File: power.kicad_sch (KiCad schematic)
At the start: 29 parts, among them IC302 L7805, IC303 L7805, Q503 BR 29, SW101 SW_SPDT

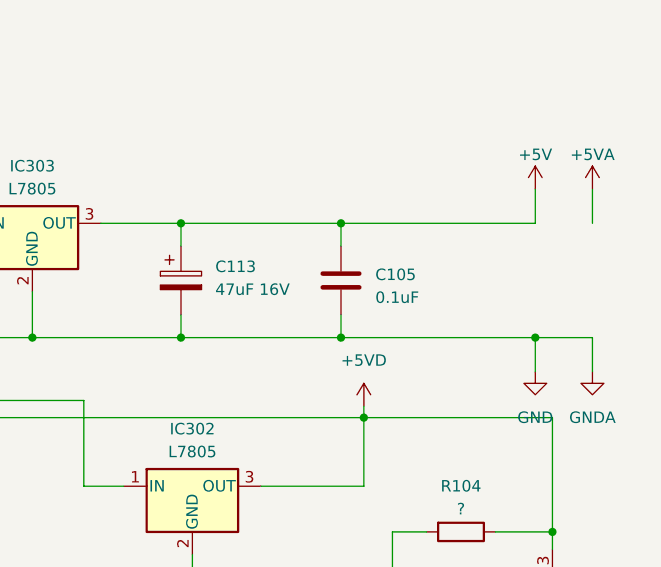
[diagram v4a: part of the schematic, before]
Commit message: IC routing mostly complete, start adding passives.
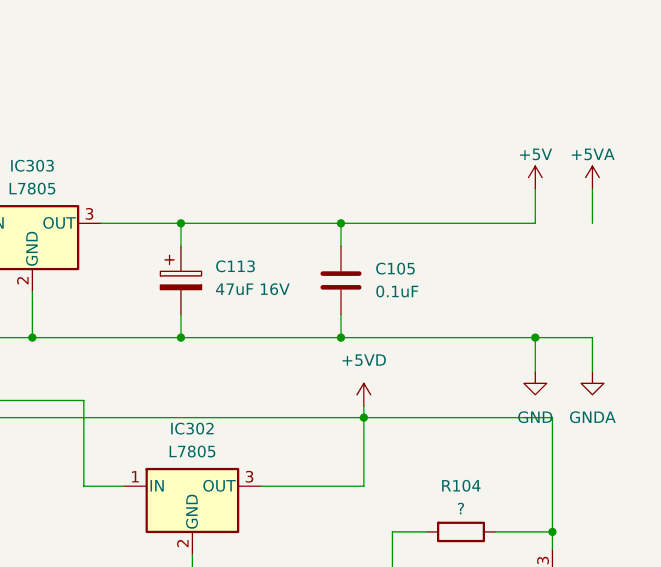
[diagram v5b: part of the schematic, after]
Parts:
- C105: footprint Capacitor_SMD:C_0805_2012Metric -> A-PCENGINE:SMD_0805_Narrow
- R104: footprint Resistor_SMD:R_0805_2012Metric -> A-PCENGINE:SMD_0805_Narrow
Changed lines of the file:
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@@
   (symbol (lib_id "Device:C") (at 287.02 57.15 0) (unit 1)
     (in_bom yes) (on_board yes) (dnp no) (fields_autoplaced)
-    (property "Reference" "C105" (at 290.83 56.515 0)
-      (effects (font (size 1.27 1.27)) (justify left))
-    )
-    (property "Value" "0.1uF" (at 290.83 59.055 0)
-      (effects (font (size 1.27 1.27)) (justify left))
-    )
-    (property "Footprint" "Capacitor_SMD:C_0805_2012Metric" (at 287.9852 60.96 0)
+    (property "Reference" "C105" (at 290.83 55.88 0)
+      (effects (font (size 1.27 1.27)) (justify left))
+    )
+    (property "Value" "0.1uF" (at 290.83 58.42 0)
+      (effects (font (size 1.27 1.27)) (justify left))
+    )
+    (property "Footprint" "A-PCENGINE:SMD_0805_Narrow" (at 287.9852 60.96 0)
       (effects (font (size 1.27 1.27)) hide)
     )
@@
         )
         (path "/c1c718c6-a427-431e-a18b-e46f94ae8e09/ba362b1f-3cb7-4861-9385-2b05dca17551"
-          (reference "C118") (unit 1)
+          (reference "Cx118") (unit 1)
         )
       )
@@
       (effects (font (size 1.27 1.27)) (justify left))
     )
-    (property "Footprint" "Capacitor_SMD:C_0805_2012Metric" (at 276.5552 139.7 0)
+    (property "Footprint" "A-PCENGINE:SMD_0805_Narrow" (at 276.5552 139.7 0)
       (effects (font (size 1.27 1.27)) hide)
     )
@@
       (effects (font (size 1.27 1.27)) (justify left))
     )
-    (property "Footprint" "Capacitor_SMD:C_0805_2012Metric" (at 235.9152 60.96 0)
+    (property "Footprint" "A-PCENGINE:SMD_0805_Narrow" (at 235.9152 60.96 0)
       (effects (font (size 1.27 1.27)) hide)
     )
@@
       (effects (font (size 1.27 1.27)) (justify left))
     )
-    (property "Footprint" "Capacitor_SMD:C_0805_2012Metric" (at 276.5552 125.73 0)
+    (property "Footprint" "A-PCENGINE:SMD_0805_Narrow" (at 276.5552 125.73 0)
       (effects (font (size 1.27 1.27)) hide)
     )
@@
       (effects (font (size 1.27 1.27)))
     )
-    (property "Footprint" "Resistor_SMD:R_0805_2012Metric" (at 300.355 83.312 90)
+    (property "Footprint" "A-PCENGINE:SMD_0805_Narrow" (at 300.355 83.312 90)
       (effects (font (size 1.27 1.27)) hide)
     )
@@
         )
         (path "/c1c718c6-a427-431e-a18b-e46f94ae8e09/ba362b1f-3cb7-4861-9385-2b05dca17551"
-          (reference "L105") (unit 1)
+          (reference "LX105") (unit 1)
         )
       )
@@
       (effects (font (size 1.27 1.27)) (justify left))
     )
-    (property "Footprint" "Capacitor_SMD:C_0805_2012Metric" (at 126.6952 60.96 0)
+    (property "Footprint" "A-PCENGINE:SMD_0805_Narrow" (at 126.6952 60.96 0)
       (effects (font (size 1.27 1.27)) hide)
     )
@@
       (effects (font (size 1.27 1.27)) (justify left))
     )
-    (property "Footprint" "Capacitor_SMD:C_0805_2012Metric" (at 221.9452 133.35 0)
+    (property "Footprint" "A-PCENGINE:SMD_0805_Narrow" (at 221.9452 133.35 0)
       (effects (font (size 1.27 1.27)) hide)
     )
@@
       (effects (font (size 1.27 1.27)))
     )
-    (property "Footprint" "Resistor_SMD:R_0805_2012Metric" (at 266.7 127.762 90)
-      (effects (font (size 1.27 1.27)) hide)
-    )
+    (property "Footprint" "A-PCENGINE:SMD_0805_Narrow" (at 266.7 127.762 90)
+      (effects (font (size 1.27 1.27)) hide)
+    )

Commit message: Bunch of passives and what-not.
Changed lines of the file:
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@@
   (junction (at 200.66 63.5) (diameter 0) (color 0 0 0 0)
+  )
+  (junction (at 308.61 50.8) (diameter 0) (color 0 0 0 0)
   )
   (junction (at 147.32 158.75) (diameter 0) (color 0 0 0 0)
@@
   )
   (wire (pts (xy 125.73 60.96) (xy 125.73 63.5))
+    (stroke (width 0) (type default))
+  )
+  (wire (pts (xy 308.61 50.8) (xy 314.96 50.8))
     (stroke (width 0) (type default))
   )
@@
   (symbol (lib_id "Device:D") (at 162.56 50.8 180) (unit 1)
     (in_bom yes) (on_board yes) (dnp no) (fields_autoplaced)
-    (property "Reference" "D101" (at 162.56 45.72 0)
-      (effects (font (size 1.27 1.27)))
-    )
-    (property "Value" "IS954" (at 162.56 48.26 0)
+    (property "Reference" "D101" (at 162.56 44.45 0)
+      (effects (font (size 1.27 1.27)))
+    )
+    (property "Value" "IS954" (at 162.56 46.99 0)
       (effects (font (size 1.27 1.27)))
     )
@@
         )
         (path "/c1c718c6-a427-431e-a18b-e46f94ae8e09/ba362b1f-3cb7-4861-9385-2b05dca17551"
-          (reference "D102") (unit 1)
-        )
-      )
+          (reference "D301") (unit 1)
+        )
+      )

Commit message: More passives, custom footprints, etc.
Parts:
- removed C113: 47uF 16V, A-PCENGINE:Elec_P5.00mm, symbol Device:C_Polarized
- added C105: ?, A-PCENGINE:SMD_0805_Narrow, symbol Device:C
- added C113: ?, A-PCENGINE:Elec_P5.00mm_D10.5mm, symbol Device:C_Polarized
- added C113: ?, A-PCENGINE:Elec_P5.00mm_D8.5mm, symbol Device:C_Polarized
- added C113: ?, A-PCENGINE:CP_8x2mm, symbol Device:C_Polarized
- added Q304: ~, A-PCENGINE:Transistor_SMD, symbol Device:Q_NPN_CBE
- C105, R104: footprint A-PCENGINE:SMD_0805_Narrow -> A-PCENGINE:SMD_0805_Narrow_Long
- C113: footprint A-PCENGINE:Elec_P5.00mm -> A-PCENGINE:Elec_P5.00mm_D8.5mm
- C113: footprint A-PCENGINE:Elec_P5.00mm -> A-PCENGINE:Elec_P5.00mm_D12.5mm
- C113: footprint A-PCENGINE:Elec_P5.00mm -> A-PCENGINE:Elec_P5.00mm_D7mm
- C113: footprint A-PCENGINE:Elec_P5.00mm -> A-PCENGINE:Elec_P5.00mm_D10.5mm
- IC302, IC303: footprint Connector_PinHeader_2.54mm:PinHeader_1x03_P2.54mm_Vertical -> A-PCENGINE:7805_Heatsink
- L106: footprint A-PCENGINE:L-5.00mm_Small_Silk -> A-PCENGINE:SMD_0805_Narrow_Long
- Q503: footprint Package_TO_SOT_SMD:SOT-23 -> A-PCENGINE:Transistor_SMD; symbol Device:Q_NPN_BEC -> Device:Q_NPN_CBE
- renumbered PX3 to P302
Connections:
- net +5V: now also L106.2, C113.1
- net +5VD: now also L106.1, Q503.1 (C); no longer Q503.3 (C)
- net GND: now also C105.1, C105.2, C113.2, C113.2, C113.2; no longer L106.1, L106.2
- net +9VA: now reaches C105.1, C113.1, C113.1, IC302.1 (IN), IC303.1 (IN), L106.2, SW101.1 (A)
- net +9VA: now also C113.1, Q304.1 (C)
- net at C113.1: now also Q304.2 (B)
- net at R104.2: now also Q503.2 (B), C113.1; no longer Q503.1 (B)
- net +5VP: now reaches C113.1
- net +5VP: now also Q304.3 (E)
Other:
- note removed: "Ground routed separately for oscillator"
- moved on the sheet: C105, C113, L101, L106, OSC901, R104

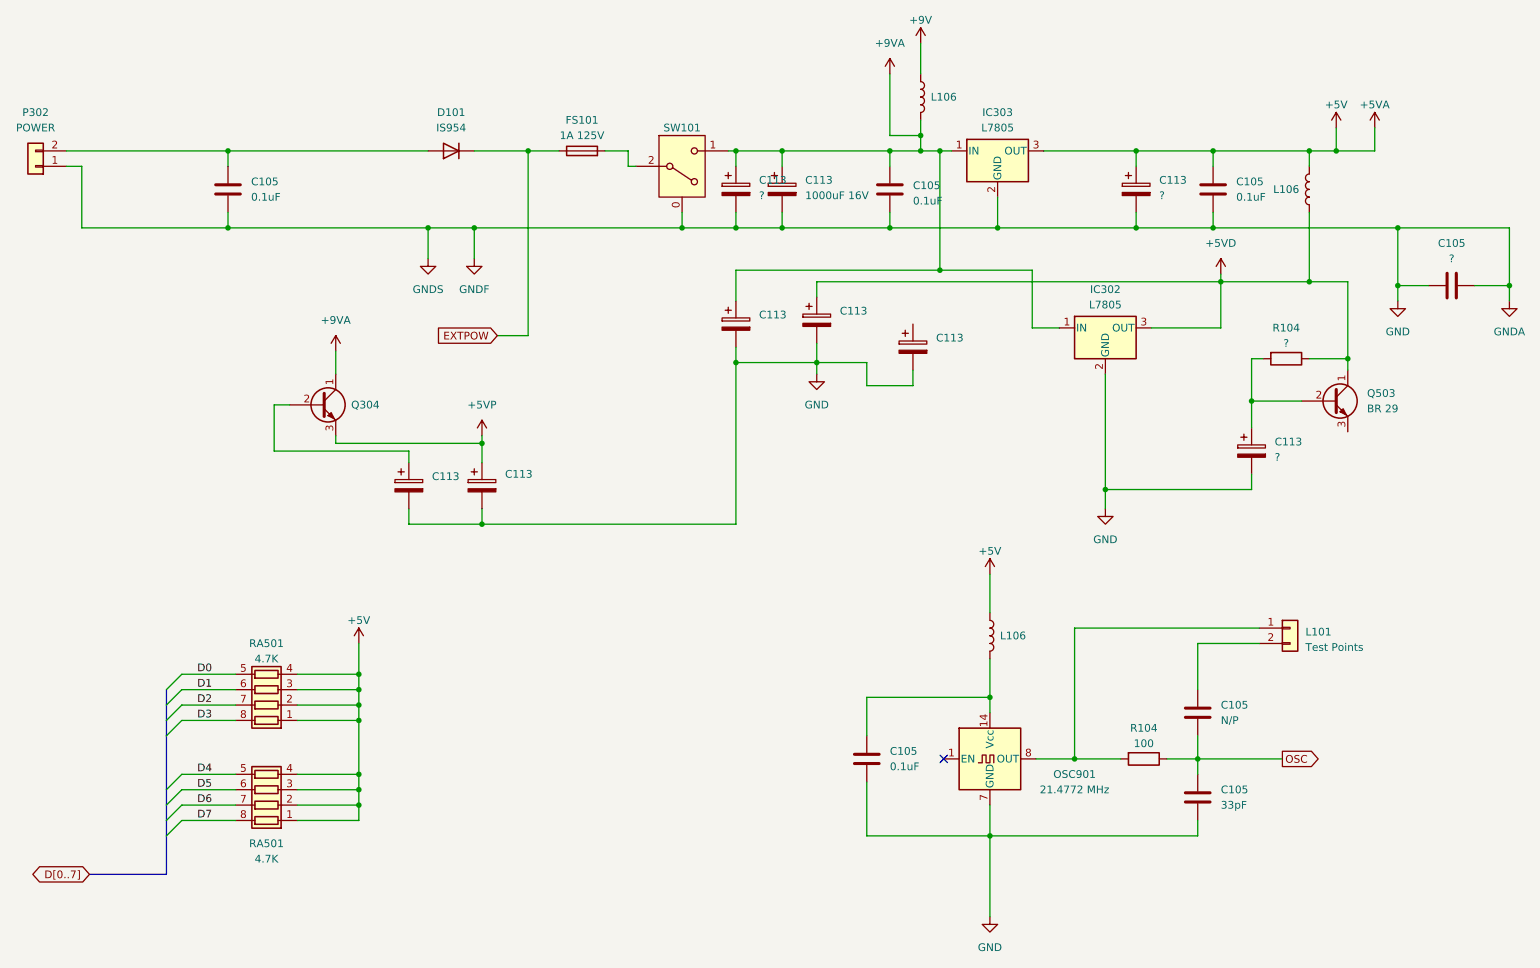
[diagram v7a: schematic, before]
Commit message: Top layer first draft.
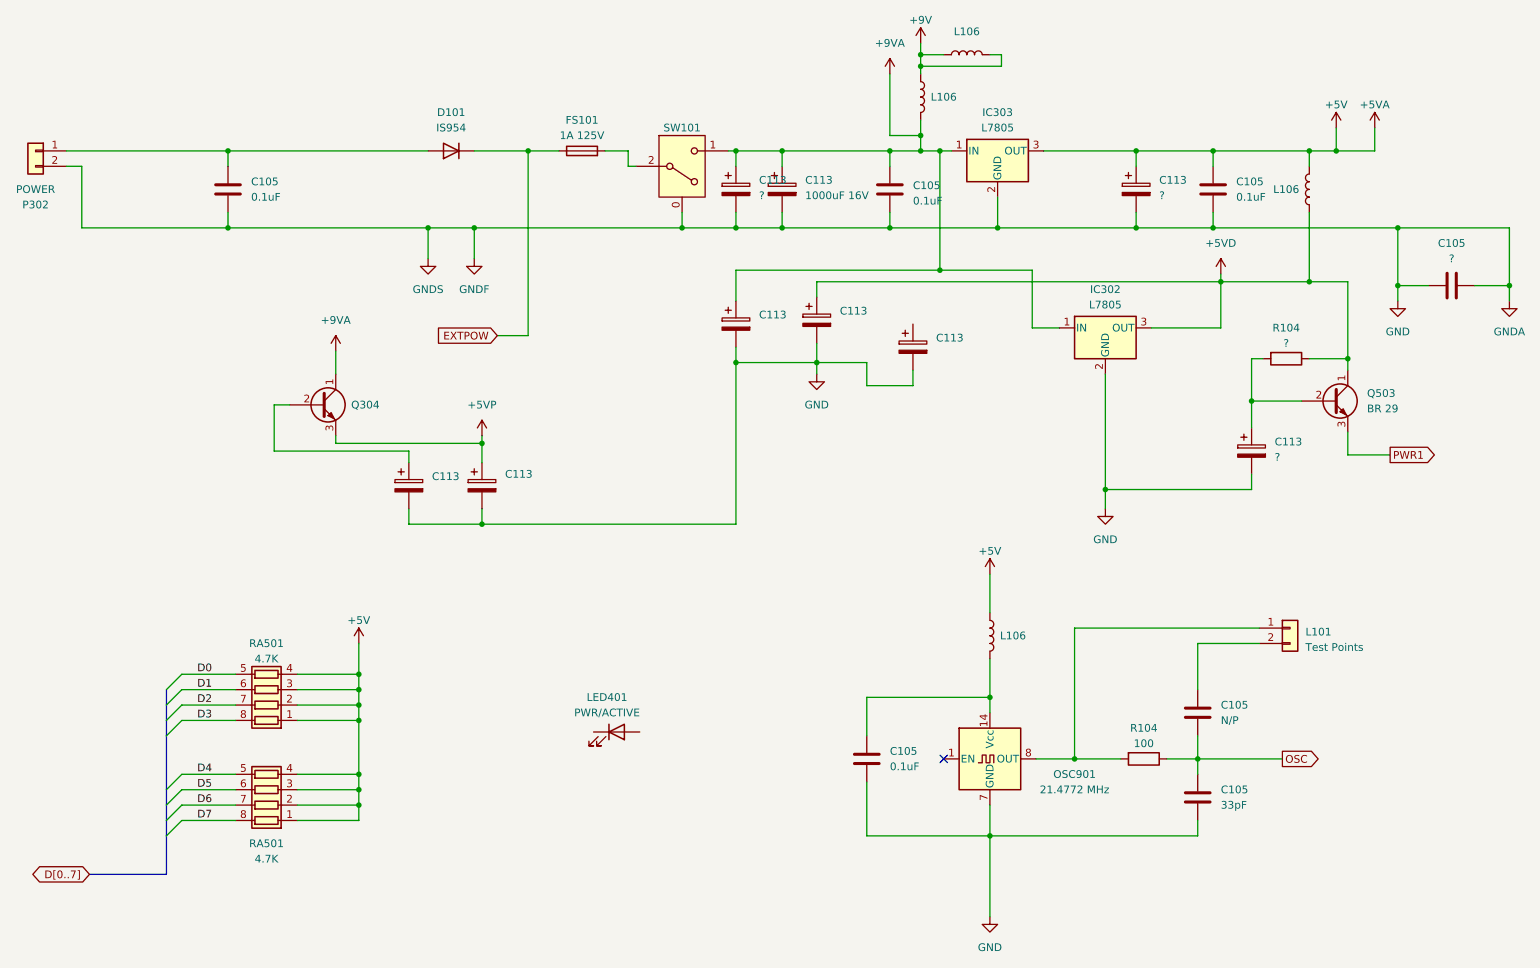
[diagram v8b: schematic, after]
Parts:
- added L106: ~, A-PCENGINE:L-5.00mm, symbol Device:L
- added LED401: PWR/ACTIVE, A-PCENGINE:Duo_LED, symbol Device:LED
- L106: footprint A-PCENGINE:L-5.00mm_Small_Silk -> A-PCENGINE:L-5.00mm
- P302: footprint Connector_PinHeader_2.00mm:PinHeader_1x02_P2.00mm_Vertical -> A-PCENGINE:Duo_Power
- RA501: footprint Resistor_SMD:R_Array_Concave_4x0603 -> A-PCENGINE:R_Array_4x0603
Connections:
- net +9V: now also L106.1, L106.2
- net GND: now also P302.2 (Pin_2); no longer P302.1 (Pin_1)
- net at C105.1, D101.2 (A): now also P302.1 (Pin_1); no longer P302.2 (Pin_2)
- net PWR1: now reaches Q503.3 (E)
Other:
- moved on the sheet: P302
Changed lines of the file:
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@@
   (junction (at 147.32 144.78) (diameter 0) (color 0 0 0 0)
   )
+  (junction (at 240.03 34.925) (diameter 0) (color 0 0 0 0)
+  )
   (junction (at 209.55 85.725) (diameter 0) (color 0 0 0 0)
+  )
+  (junction (at 240.03 36.83) (diameter 0) (color 0 0 0 0)
   )
   (junction (at 167.64 112.395) (diameter 0) (color 0 0 0 0)
@@
     (stroke (width 0) (type default))
   )
+  (wire (pts (xy 253.365 34.925) (xy 251.46 34.925))
+    (stroke (width 0) (type default))
+  )
   (wire (pts (xy 294.64 85.09) (xy 296.545 85.09))
     (stroke (width 0) (type default))
@@
     (stroke (width 0) (type default))
   )
+  (wire (pts (xy 240.03 36.83) (xy 240.03 38.1))
+    (stroke (width 0) (type default))
+  )
   (wire (pts (xy 137.16 156.21) (xy 147.32 156.21))
     (stroke (width 0) (type default))
@@
     (stroke (width 0) (type default))
   )
-  (wire (pts (xy 240.03 33.02) (xy 240.03 38.1))
+  (wire (pts (xy 240.03 33.02) (xy 240.03 34.925))
+    (stroke (width 0) (type default))
+  )
+  (wire (pts (xy 253.365 36.83) (xy 253.365 34.925))
     (stroke (width 0) (type default))
   )
@@
     (stroke (width 0) (type default))
   )
+  (wire (pts (xy 240.03 34.925) (xy 243.84 34.925))
+    (stroke (width 0) (type default))
+  )
   (wire (pts (xy 125.73 60.96) (xy 125.73 63.5))
     (stroke (width 0) (type default))
@@
     (stroke (width 0) (type default))
   )
+  (wire (pts (xy 240.03 34.925) (xy 240.03 36.83))
+    (stroke (width 0) (type default))
+  )
   (wire (pts (xy 231.14 163.83) (xy 251.46 163.83))
     (stroke (width 0) (type default))
@@
     (stroke (width 0) (type default))
   )
+  (wire (pts (xy 310.515 100.965) (xy 317.5 100.965))
+    (stroke (width 0) (type default))
+  )
   (wire (pts (xy 251.46 140.97) (xy 231.14 140.97))
     (stroke (width 0) (type default))
@@
     (stroke (width 0) (type default))
   )
+  (wire (pts (xy 310.515 97.155) (xy 310.515 100.965))
+    (stroke (width 0) (type default))
+  )
   (wire (pts (xy 155.575 109.855) (xy 155.575 112.395))
     (stroke (width 0) (type default))
@@
   )
   (wire (pts (xy 209.55 60.96) (xy 209.55 63.5))
+    (stroke (width 0) (type default))
+  )
+  (wire (pts (xy 240.03 36.83) (xy 253.365 36.83))
     (stroke (width 0) (type default))
   )
@@
     )
   )
+  (global_label "PWR1" (shape output) (at 317.5 100.965 0) (fields_autoplaced)
+    (effects (font (size 1.27 1.27)) (justify left))
+    (property "Intersheetrefs" "${INTERSHEET_REFS}" (at 325.6861 100.965 0)
+      (effects (font (size 1.27 1.27)) (justify left) hide)
+    )
+  )
   (symbol (lib_id "power:GND") (at 251.46 177.165 0) (unit 1)
     (in_bom yes) (on_board yes) (dnp no) (fields_autoplaced)
@@
     )
   )
+  (symbol (lib_id "Device:LED") (at 189.865 146.685 0) (unit 1)
+    (in_bom yes) (on_board yes) (dnp no) (fields_autoplaced)
+    (property "Reference" "LED401" (at 188.2775 140.97 0)
+      (effects (font (size 1.27 1.27)))
+    )
+    (property "Value" "PWR/ACTIVE" (at 188.2775 143.51 0)
+      (effects (font (size 1.27 1.27)))
+    )
+    (property "Footprint" "A-PCENGINE:Duo_LED" (at 189.865 146.685 0)
+      (effects (font (size 1.27 1.27)) hide)
+    )
+    (property "Datasheet" "~" (at 189.865 146.685 0)
+      (effects (font (size 1.27 1.27)) hide)
+    )
+    (pin "1")
+    (pin "2")
+    (instances
+      (project "PCE"
+        (path "/c1c718c6-a427-431e-a18b-e46f94ae8e09/ba362b1f-3cb7-4861-9385-2b05dca17551"
+          (reference "LED401") (unit 1)
+        )
+      )
+    )
+  )
   (symbol (lib_id "Device:C") (at 125.73 57.15 0) (unit 1)
     (in_bom yes) (on_board yes) (dnp no) (fields_autoplaced)
@@
       (effects (font (size 1.27 1.27)))
     )
-    (property "Footprint" "Resistor_SMD:R_Array_Concave_4x0603" (at 132.08 132.715 90)
+    (property "Footprint" "A-PCENGINE:R_Array_4x0603" (at 132.08 132.715 90)
       (effects (font (size 1.27 1.27)) hide)
     )
@@
       (effects (font (size 1.27 1.27)))
     )
-    (property "Footprint" "A-PCENGINE:L-5.00mm_Small_Silk" (at 240.03 41.91 0)
+    (property "Footprint" "A-PCENGINE:L-5.00mm" (at 240.03 41.91 0)
       (effects (font (size 1.27 1.27)) hide)
     )
@@
       (effects (font (size 1.27 1.27)))
     )
-    (property "Footprint" "Resistor_SMD:R_Array_Concave_4x0603" (at 132.08 149.225 90)
+    (property "Footprint" "A-PCENGINE:R_Array_4x0603" (at 132.08 149.225 90)
       (effects (font (size 1.27 1.27)) hide)
     )
@@
     )
   )
-  (symbol (lib_id "Connector_Generic:Conn_01x02") (at 93.98 53.34 180) (unit 1)
-    (in_bom yes) (on_board yes) (dnp no)
-    (property "Reference" "P302" (at 93.98 44.45 0)
-      (effects (font (size 1.27 1.27)))
-    )
-    (property "Value" "POWER" (at 93.98 46.99 0)
-      (effects (font (size 1.27 1.27)))
-    )
-    (property "Footprint" "Connector_PinHeader_2.00mm:PinHeader_1x02_P2.00mm_Vertical" (at 93.98 53.34 0)
-      (effects (font (size 1.27 1.27)) hide)
-    )
-    (property "Datasheet" "~" (at 93.98 53.34 0)
+  (symbol (lib_id "Connector_Generic:Conn_01x02") (at 93.98 50.8 0) (mirror y) (unit 1)
+    (in_bom yes) (on_board yes) (dnp no)
+    (property "Reference" "P302" (at 93.98 59.69 0)
+      (effects (font (size 1.27 1.27)))
+    )
+    (property "Value" "POWER" (at 93.98 57.15 0)
+      (effects (font (size 1.27 1.27)))
+    )
+    (property "Footprint" "A-PCENGINE:Duo_Power" (at 93.98 50.8 0)
+      (effects (font (size 1.27 1.27)) hide)
+    )
+    (property "Datasheet" "~" (at 93.98 50.8 0)
       (effects (font (size 1.27 1.27)) hide)
     )
@@
       (effects (font (size 1.27 1.27)))
     )
-    (property "Footprint" "A-PCENGINE:L-5.00mm_Small_Silk" (at 251.46 130.81 0)
+    (property "Footprint" "A-PCENGINE:L-5.00mm" (at 251.46 130.81 0)
       (effects (font (size 1.27 1.27)) hide)
     )
@@
         )
       )
+    )
+  )
+  (symbol (lib_id "Device:L") (at 247.65 34.925 90) (unit 1)
+    (in_bom yes) (on_board yes) (dnp no)
+    (property "Reference" "L106" (at 247.65 31.115 90)
+      (effects (font (size 1.27 1.27)))
+    )
+    (property "Value" "~" (at 247.65 33.655 90)
+      (effects (font (size 1.27 1.27)))
+    )
+    (property "Footprint" "A-PCENGINE:L-5.00mm" (at 247.65 34.925 0)
+      (effects (font (size 1.27 1.27)) hide)
+    )
+    (property "Datasheet" "~" (at 247.65 34.925 0)
+      (effects (font (size 1.27 1.27)) hide)
+    )
+    (pin "1")
+    (pin "2")
+    (instances
+      (project "PCE"
+        (path "/c1c718c6-a427-431e-a18b-e46f94ae8e09/c78d7e8a-3e65-46f4-91f4-96eb31925bea"
+          (reference "L106") (unit 1)
+        )
+        (path "/c1c718c6-a427-431e-a18b-e46f94ae8e09/ba362b1f-3cb7-4861-9385-2b05dca17551"
+          (reference "L107") (unit 1)
+        )
+        (path "/c1c718c6-a427-431e-a18b-e46f94ae8e09/99dc3156-542f-4db3-aeb5-d38a9dd48b1b"
+          (reference "L1") (unit 1)
+        )
+      )
